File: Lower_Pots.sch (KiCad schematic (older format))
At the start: 17 parts, among them U6 CD74HC4067M

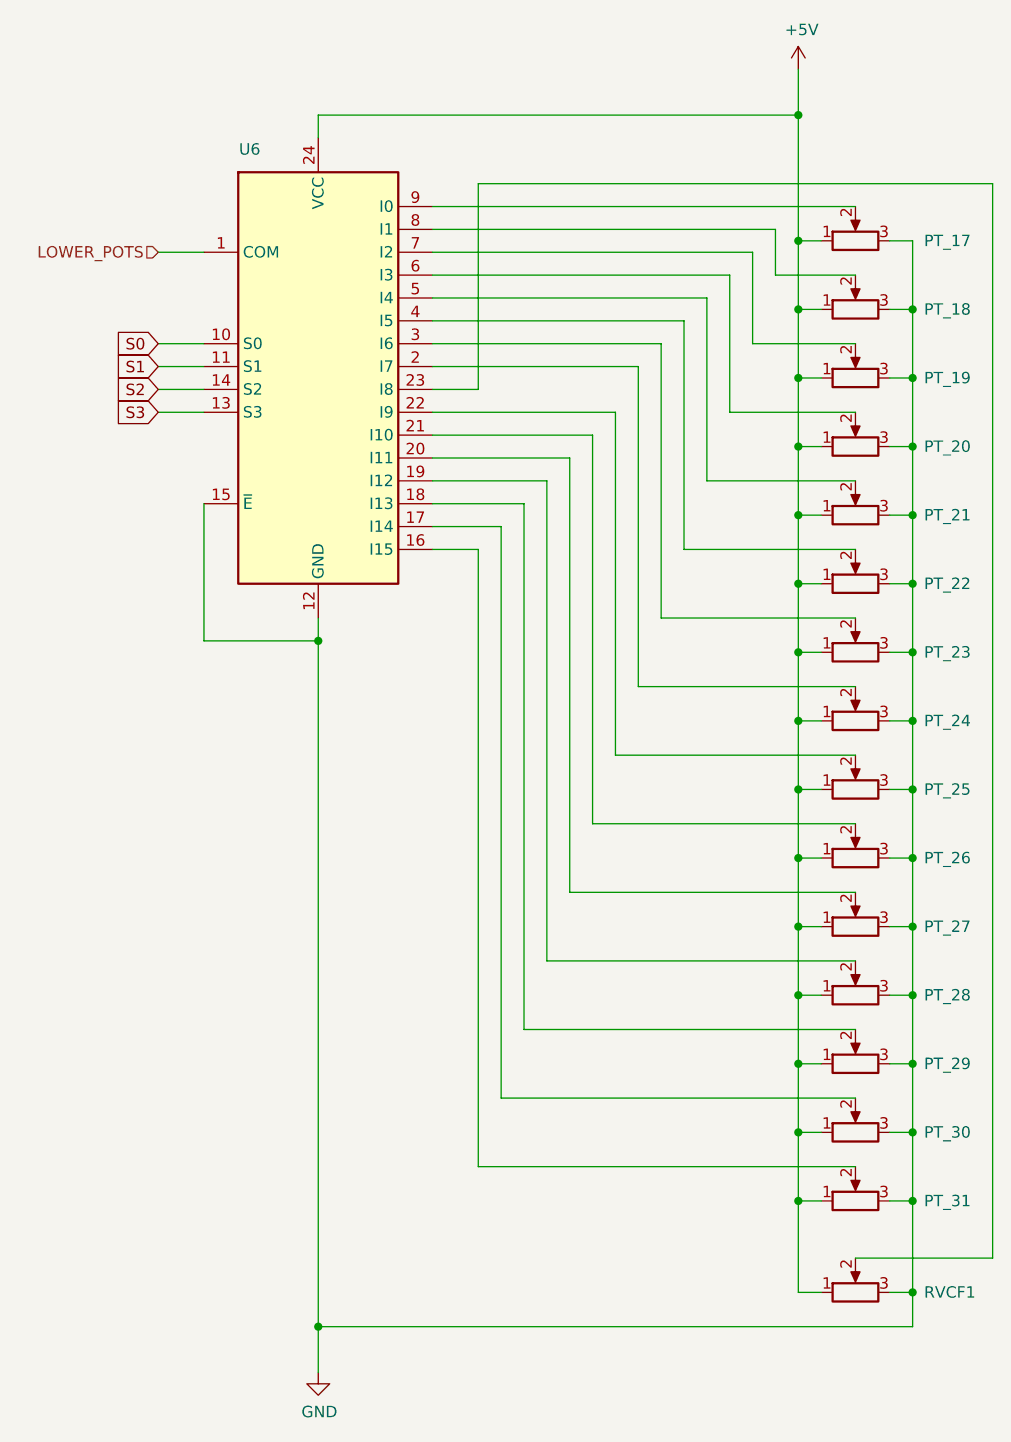
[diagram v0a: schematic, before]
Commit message: Updated Schematic and changed rotary pots
Better button symbol and flipped all rotary pots in the schematic so they've connected the right way round.

Changed the rotary pot footprints so the graphics match the ones I'm using.
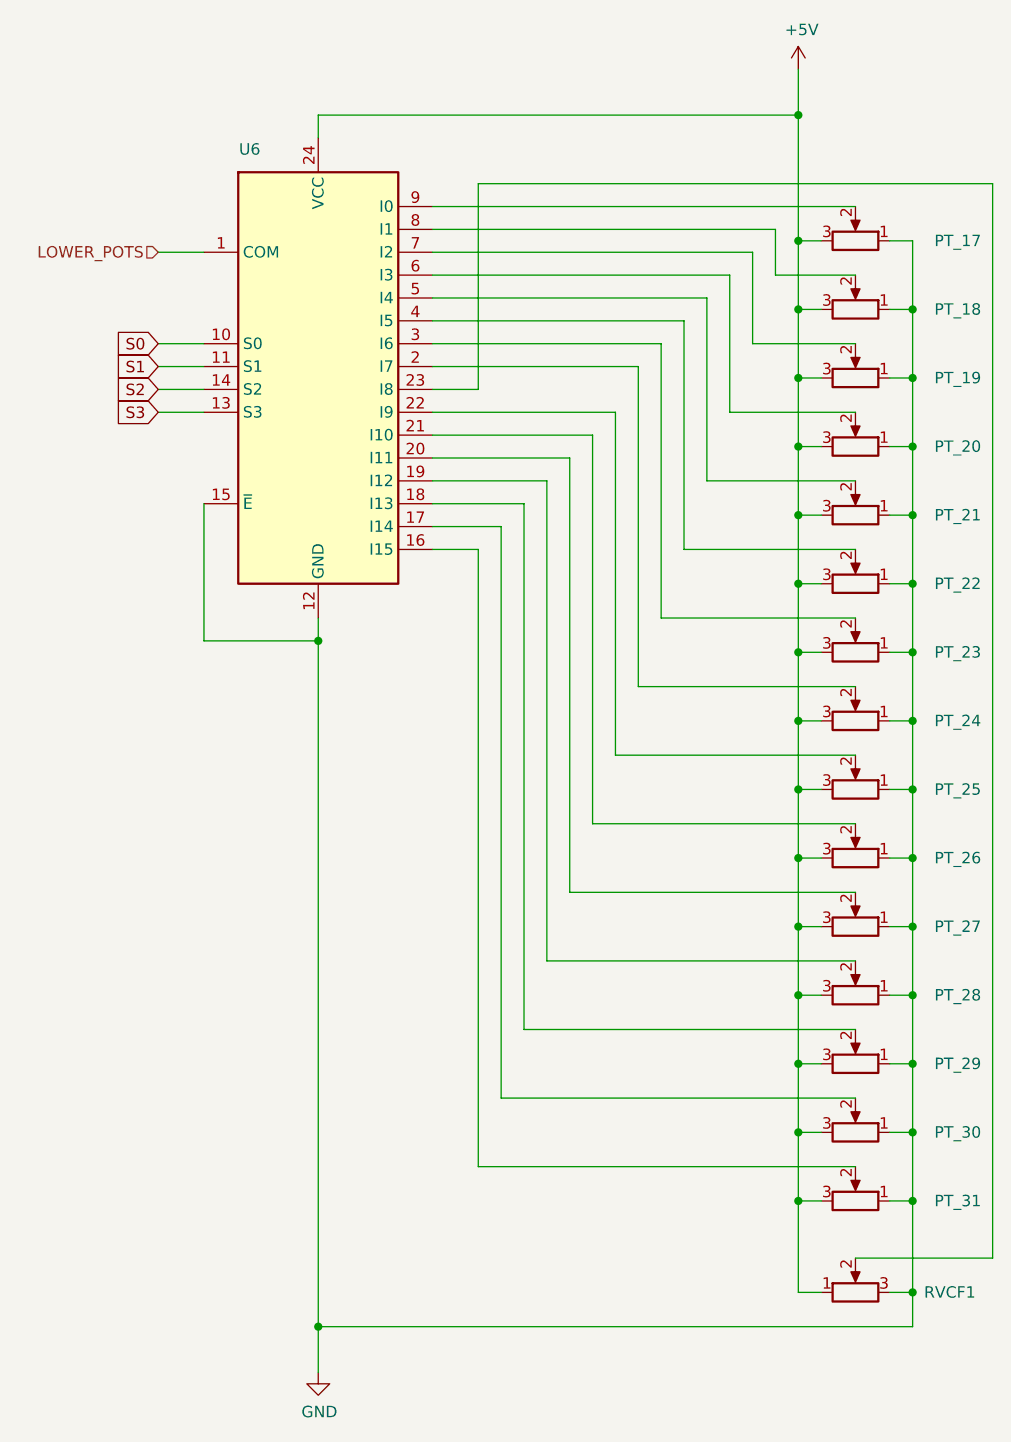
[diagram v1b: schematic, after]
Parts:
- PT_17, PT_18, PT_19, PT_20, PT_21, PT_22, PT_23, PT_24, PT_25, PT_26, PT_27, PT_28, PT_29, PT_30, PT_31: footprint cunabulapress-footprints:Potentiometer_Alps_RK09K_Single_Vertical_Edit -> cunabulapress-footprints:Potentiometer_Alps_RK09D1130X
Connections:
- net +5V: now also PT_17.3, PT_18.3, PT_19.3, PT_20.3, PT_21.3, PT_22.3, PT_23.3, PT_24.3, PT_25.3, PT_26.3, PT_27.3, PT_28.3, PT_29.3, PT_30.3, PT_31.3; no longer PT_17.1, PT_18.1, PT_19.1, PT_20.1, PT_21.1, PT_22.1, PT_23.1, PT_24.1, PT_25.1, PT_26.1, PT_27.1, PT_28.1, PT_29.1, PT_30.1, PT_31.1
- net GND: now also PT_17.1, PT_18.1, PT_19.1, PT_20.1, PT_21.1, PT_22.1, PT_23.1, PT_24.1, PT_25.1, PT_26.1, PT_27.1, PT_28.1, PT_29.1, PT_30.1, PT_31.1; no longer PT_17.3, PT_18.3, PT_19.3, PT_20.3, PT_21.3, PT_22.3, PT_23.3, PT_24.3, PT_25.3, PT_26.3, PT_27.3, PT_28.3, PT_29.3, PT_30.3, PT_31.3
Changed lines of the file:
@@
 EESchema Schematic File Version 4
 LIBS:cp_midi_control_surface_002-cache
-EELAYER 30 0
+EELAYER 26 0
 EELAYER END
 $Descr A4 11693 8268
@@
 AR Path="/5C3B66BD/5C49B48A" Ref="PT_?"  Part="1"
 AR Path="/5C504054/5C49B48A" Ref="PT_17"  Part="1"
-F 0 "PT_17" V 5050 1400 50  0000 R CNN
+F 0 "PT_17" V 5050 2250 50  0000 R CNN
 F 1 "10k" H 4980 1655 50  0001 R CNN
-F 2 "cunabulapress-footprints:Potentiometer_Alps_RK09K_Single_Vertical_Edit" H 5050 1700 50  0001 C CNN
+F 2 "cunabulapress-footprints:Potentiometer_Alps_RK09D1130X" H 5050 1700 50  0001 C CNN
 F 3 "~" H 5050 1700 50  0001 C CNN
 	1    5050 1700
-	0    -1   -1   0
+	0    1    -1   0
 $EndComp
 $Comp
@@
 AR Path="/5C3B66BD/5C49B491" Ref="PT_?"  Part="1"
 AR Path="/5C504054/5C49B491" Ref="PT_18"  Part="1"
-F 0 "PT_18" V 5050 1700 50  0000 R CNN
+F 0 "PT_18" V 5050 2550 50  0000 R CNN
 F 1 "10k" H 4980 1955 50  0001 R CNN
-F 2 "cunabulapress-footprints:Potentiometer_Alps_RK09K_Single_Vertical_Edit" H 5050 2000 50  0001 C CNN
+F 2 "cunabulapress-footprints:Potentiometer_Alps_RK09D1130X" H 5050 2000 50  0001 C CNN
 F 3 "~" H 5050 2000 50  0001 C CNN
 	1    5050 2000
-	0    -1   -1   0
+	0    1    -1   0
 $EndComp
 $Comp
@@
 AR Path="/5C3B66BD/5C49B498" Ref="PT_?"  Part="1"
 AR Path="/5C504054/5C49B498" Ref="PT_19"  Part="1"
-F 0 "PT_19" V 5050 2000 50  0000 R CNN
+F 0 "PT_19" V 5050 2850 50  0000 R CNN
 F 1 "10k" H 4980 2255 50  0001 R CNN
-F 2 "cunabulapress-footprints:Potentiometer_Alps_RK09K_Single_Vertical_Edit" H 5050 2300 50  0001 C CNN
+F 2 "cunabulapress-footprints:Potentiometer_Alps_RK09D1130X" H 5050 2300 50  0001 C CNN
 F 3 "~" H 5050 2300 50  0001 C CNN
 	1    5050 2300
-	0    -1   -1   0
+	0    1    -1   0
 $EndComp
 $Comp
@@
 AR Path="/5C3B66BD/5C49B49F" Ref="PT_?"  Part="1"
 AR Path="/5C504054/5C49B49F" Ref="PT_20"  Part="1"
-F 0 "PT_20" V 5050 2300 50  0000 R CNN
+F 0 "PT_20" V 5050 3150 50  0000 R CNN
 F 1 "10k" H 4980 2555 50  0001 R CNN
-F 2 "cunabulapress-footprints:Potentiometer_Alps_RK09K_Single_Vertical_Edit" H 5050 2600 50  0001 C CNN
+F 2 "cunabulapress-footprints:Potentiometer_Alps_RK09D1130X" H 5050 2600 50  0001 C CNN
 F 3 "~" H 5050 2600 50  0001 C CNN
 	1    5050 2600
-	0    -1   -1   0
+	0    1    -1   0
 $EndComp
 $Comp
@@
 AR Path="/5C3B66BD/5C49B4A6" Ref="PT_?"  Part="1"
 AR Path="/5C504054/5C49B4A6" Ref="PT_21"  Part="1"
-F 0 "PT_21" V 5050 2600 50  0000 R CNN
+F 0 "PT_21" V 5050 3450 50  0000 R CNN
 F 1 "10k" V 5050 2900 50  0001 C CNN
-F 2 "cunabulapress-footprints:Potentiometer_Alps_RK09K_Single_Vertical_Edit" H 5050 2900 50  0001 C CNN
+F 2 "cunabulapress-footprints:Potentiometer_Alps_RK09D1130X" H 5050 2900 50  0001 C CNN
 F 3 "~" H 5050 2900 50  0001 C CNN
 	1    5050 2900
-	0    -1   -1   0
+	0    1    -1   0
 $EndComp
 $Comp
@@
 AR Path="/5C3B66BD/5C49B4AD" Ref="PT_?"  Part="1"
 AR Path="/5C504054/5C49B4AD" Ref="PT_22"  Part="1"
-F 0 "PT_22" V 5050 2900 50  0000 R CNN
+F 0 "PT_22" V 5050 3750 50  0000 R CNN
 F 1 "10k" H 4980 3155 50  0001 R CNN
-F 2 "cunabulapress-footprints:Potentiometer_Alps_RK09K_Single_Vertical_Edit" H 5050 3200 50  0001 C CNN
+F 2 "cunabulapress-footprints:Potentiometer_Alps_RK09D1130X" H 5050 3200 50  0001 C CNN
 F 3 "~" H 5050 3200 50  0001 C CNN
 	1    5050 3200
-	0    -1   -1   0
+	0    1    -1   0
 $EndComp
 $Comp
@@
 AR Path="/5C3B66BD/5C49B4B4" Ref="PT_?"  Part="1"
 AR Path="/5C504054/5C49B4B4" Ref="PT_23"  Part="1"
-F 0 "PT_23" V 5050 3200 50  0000 R CNN
+F 0 "PT_23" V 5050 4050 50  0000 R CNN
 F 1 "10k" H 4980 3455 50  0001 R CNN
-F 2 "cunabulapress-footprints:Potentiometer_Alps_RK09K_Single_Vertical_Edit" H 5050 3500 50  0001 C CNN
+F 2 "cunabulapress-footprints:Potentiometer_Alps_RK09D1130X" H 5050 3500 50  0001 C CNN
 F 3 "~" H 5050 3500 50  0001 C CNN
 	1    5050 3500
-	0    -1   -1   0
+	0    1    -1   0
 $EndComp
 $Comp
@@
 AR Path="/5C3B66BD/5C49B4BB" Ref="PT_?"  Part="1"
 AR Path="/5C504054/5C49B4BB" Ref="PT_24"  Part="1"
-F 0 "PT_24" V 5050 3500 50  0000 R CNN
+F 0 "PT_24" V 5050 4350 50  0000 R CNN
 F 1 "10k" H 4980 3755 50  0001 R CNN
-F 2 "cunabulapress-footprints:Potentiometer_Alps_RK09K_Single_Vertical_Edit" H 5050 3800 50  0001 C CNN
+F 2 "cunabulapress-footprints:Potentiometer_Alps_RK09D1130X" H 5050 3800 50  0001 C CNN
 F 3 "~" H 5050 3800 50  0001 C CNN
 	1    5050 3800
-	0    -1   -1   0
+	0    1    -1   0
 $EndComp
 $Comp
@@
 AR Path="/5C3B66BD/5C49B4C2" Ref="PT_?"  Part="1"
 AR Path="/5C504054/5C49B4C2" Ref="PT_25"  Part="1"
-F 0 "PT_25" V 5050 3800 50  0000 R CNN
+F 0 "PT_25" V 5050 4650 50  0000 R CNN
 F 1 "10k" H 4980 4055 50  0001 R CNN
-F 2 "cunabulapress-footprints:Potentiometer_Alps_RK09K_Single_Vertical_Edit" H 5050 4100 50  0001 C CNN
+F 2 "cunabulapress-footprints:Potentiometer_Alps_RK09D1130X" H 5050 4100 50  0001 C CNN
 F 3 "~" H 5050 4100 50  0001 C CNN
 	1    5050 4100
-	0    -1   -1   0
+	0    1    -1   0
 $EndComp
 $Comp
@@
 AR Path="/5C3B66BD/5C49B4C9" Ref="PT_?"  Part="1"
 AR Path="/5C504054/5C49B4C9" Ref="PT_26"  Part="1"
-F 0 "PT_26" V 5050 4100 50  0000 R CNN
+F 0 "PT_26" V 5050 4950 50  0000 R CNN
 F 1 "10k" H 4980 4355 50  0001 R CNN
-F 2 "cunabulapress-footprints:Potentiometer_Alps_RK09K_Single_Vertical_Edit" H 5050 4400 50  0001 C CNN
+F 2 "cunabulapress-footprints:Potentiometer_Alps_RK09D1130X" H 5050 4400 50  0001 C CNN
 F 3 "~" H 5050 4400 50  0001 C CNN
 	1    5050 4400
-	0    -1   -1   0
+	0    1    -1   0
 $EndComp
 $Comp
@@
 AR Path="/5C3B66BD/5C49B4D0" Ref="PT_?"  Part="1"
 AR Path="/5C504054/5C49B4D0" Ref="PT_27"  Part="1"
-F 0 "PT_27" V 5050 4400 50  0000 R CNN
+F 0 "PT_27" V 5050 5250 50  0000 R CNN
 F 1 "10k" H 4980 4655 50  0001 R CNN
-F 2 "cunabulapress-footprints:Potentiometer_Alps_RK09K_Single_Vertical_Edit" H 5050 4700 50  0001 C CNN
+F 2 "cunabulapress-footprints:Potentiometer_Alps_RK09D1130X" H 5050 4700 50  0001 C CNN
 F 3 "~" H 5050 4700 50  0001 C CNN
 	1    5050 4700
-	0    -1   -1   0
+	0    1    -1   0
 $EndComp
 $Comp
@@
 AR Path="/5C3B66BD/5C49B4D7" Ref="PT_?"  Part="1"
 AR Path="/5C504054/5C49B4D7" Ref="PT_28"  Part="1"
-F 0 "PT_28" V 5050 4700 50  0000 R CNN
+F 0 "PT_28" V 5050 5550 50  0000 R CNN
 F 1 "10k" H 4980 4955 50  0001 R CNN
-F 2 "cunabulapress-footprints:Potentiometer_Alps_RK09K_Single_Vertical_Edit" H 5050 5000 50  0001 C CNN
+F 2 "cunabulapress-footprints:Potentiometer_Alps_RK09D1130X" H 5050 5000 50  0001 C CNN
 F 3 "~" H 5050 5000 50  0001 C CNN
 	1    5050 5000
-	0    -1   -1   0
+	0    1    -1   0
 $EndComp
 $Comp
@@
 AR Path="/5C3B66BD/5C62451C" Ref="PT_?"  Part="1"
 AR Path="/5C504054/5C62451C" Ref="PT_29"  Part="1"
-F 0 "PT_29" V 5050 5000 50  0000 R CNN
+F 0 "PT_29" V 5050 5850 50  0000 R CNN
 F 1 "10k" H 4980 5255 50  0001 R CNN
-F 2 "cunabulapress-footprints:Potentiometer_Alps_RK09K_Single_Vertical_Edit" H 5050 5300 50  0001 C CNN
+F 2 "cunabulapress-footprints:Potentiometer_Alps_RK09D1130X" H 5050 5300 50  0001 C CNN
 F 3 "~" H 5050 5300 50  0001 C CNN
 	1    5050 5300
-	0    -1   -1   0
+	0    1    -1   0
 $EndComp
 $Comp
@@
 AR Path="/5C3B66BD/5C624522" Ref="PT_?"  Part="1"
 AR Path="/5C504054/5C624522" Ref="PT_30"  Part="1"
-F 0 "PT_30" V 5050 5300 50  0000 R CNN
+F 0 "PT_30" V 5050 6150 50  0000 R CNN
 F 1 "10k" H 4980 5555 50  0001 R CNN
-F 2 "cunabulapress-footprints:Potentiometer_Alps_RK09K_Single_Vertical_Edit" H 5050 5600 50  0001 C CNN
+F 2 "cunabulapress-footprints:Potentiometer_Alps_RK09D1130X" H 5050 5600 50  0001 C CNN
 F 3 "~" H 5050 5600 50  0001 C CNN
 	1    5050 5600
-	0    -1   -1   0
+	0    1    -1   0
 $EndComp
 $Comp
@@
 AR Path="/5C3B66BD/5C624528" Ref="PT_?"  Part="1"
 AR Path="/5C504054/5C624528" Ref="PT_31"  Part="1"
-F 0 "PT_31" V 5050 5600 50  0000 R CNN
+F 0 "PT_31" V 5050 6450 50  0000 R CNN
 F 1 "10k" H 4980 5855 50  0001 R CNN
-F 2 "cunabulapress-footprints:Potentiometer_Alps_RK09K_Single_Vertical_Edit" H 5050 5900 50  0001 C CNN
+F 2 "cunabulapress-footprints:Potentiometer_Alps_RK09D1130X" H 5050 5900 50  0001 C CNN
 F 3 "~" H 5050 5900 50  0001 C CNN
 	1    5050 5900
-	0    -1   -1   0
-$EndComp
-Wire Wire Line
+	0    1    -1   0
+$EndComp
+Wire Wire Line
